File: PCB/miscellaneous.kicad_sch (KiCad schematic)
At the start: 34 parts

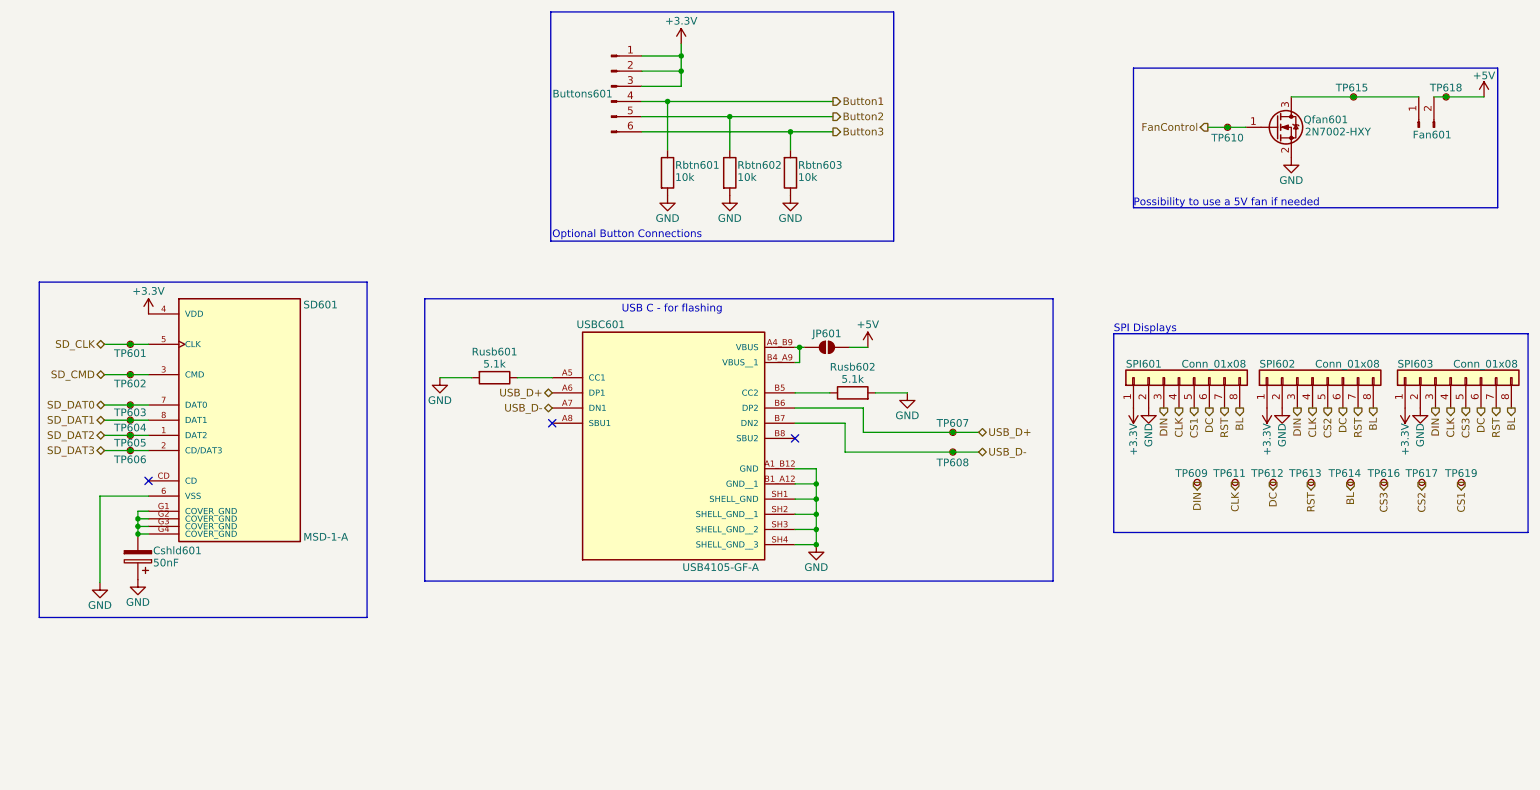
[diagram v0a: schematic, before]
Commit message: Applied recommendations from my coworker; Fixed badly placed filter caps; Added flyback diode to fan circuit; Applied larger grid and some spacing to the schematics; And some other small adjustments
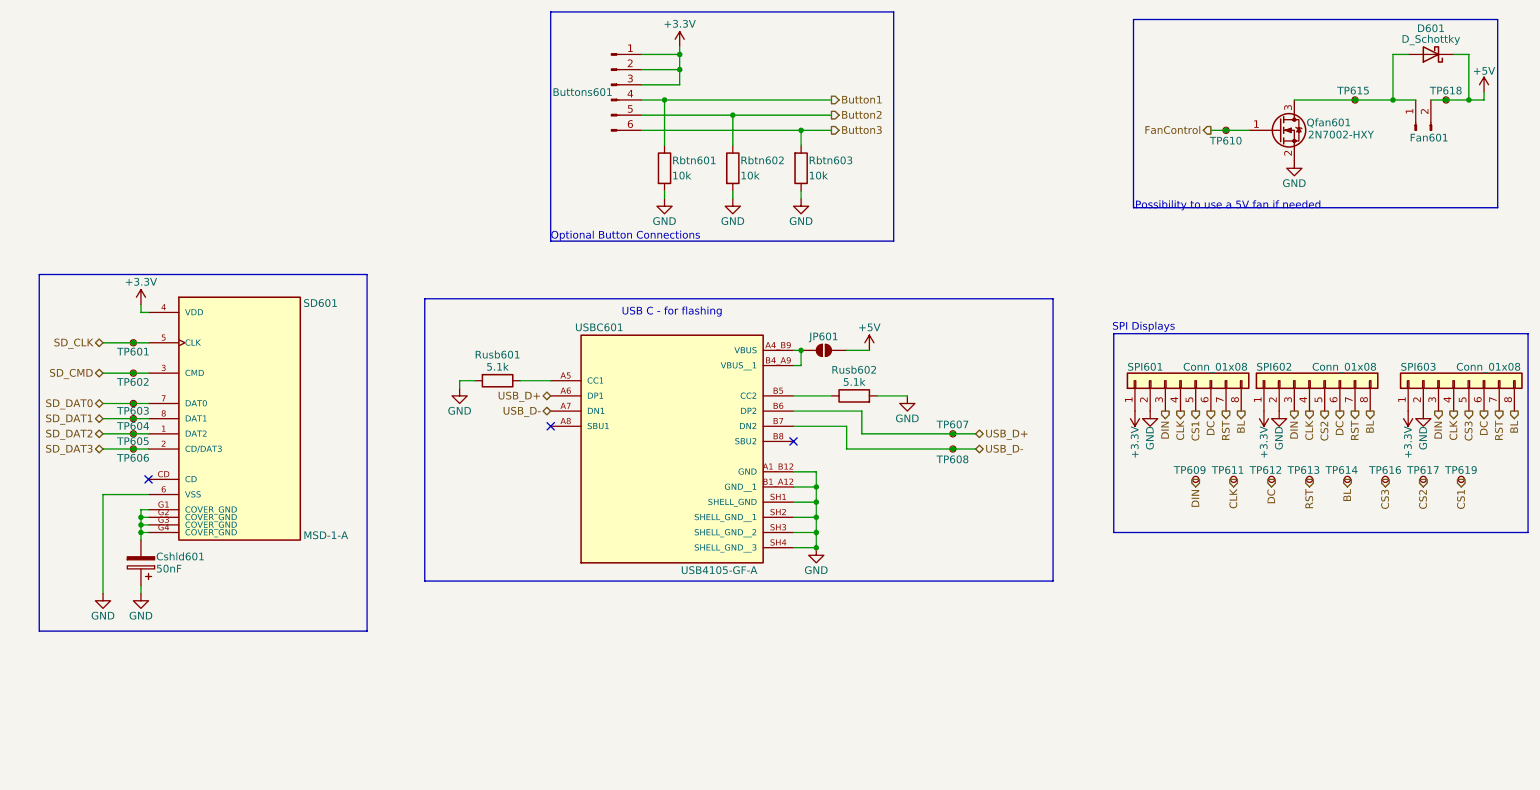
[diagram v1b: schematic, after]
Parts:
- added D601: D_Schottky, Diode_SMD:D_0805_2012Metric, symbol Device:D_Schottky
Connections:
- net +5V: now also D601.1 (K)
- net at Fan601.1 (Pin_1), Qfan601.3 (D), TP615.1: now also D601.2 (A)
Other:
- title: (none) -> Miscellaneous
- moved on the sheet: Cshld601, Fan601, JP601, Qfan601, Rbtn601, Rbtn602, Rbtn603, Rusb601, Rusb602, SPI601, SPI602, SPI603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

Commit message: Changed some resistor and capacitor values;Added additional input electrolytic cap;Selected LCSC parts;Added diode footprint;Removed 3.3V power supply and decreased the output of the 5V supply to 3.3V;Added flyback diode on the fan circuit;Added LDO between the USB-C VBUS and the 5V rail
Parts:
- removed TP618: TestPoint_Small, TestPoint:TestPoint_Pad_D1.0mm, symbol Connector:TestPoint_Small
- added C601: 10uF, Capacitor_SMD:C_0805_2012Metric, symbol Device:C
- added C602: 22uF, Capacitor_SMD:C_0805_2012Metric, symbol Device:C
- added U601: AMS1117-3.3, Package_TO_SOT_SMD:SOT-223-3_TabPin2, symbol Regulator_Linear:AMS1117-3.3
- D601: footprint Diode_SMD:D_0805_2012Metric -> customFootprints:SOD-323HE
- renumbered TP609 to TP601, TP611 to TP602, TP601 to TP603, TP602 to TP604, TP603 to TP605, TP604 to TP606, TP605 to TP607, TP606 to TP608, TP612 to TP609, TP613 to TP610, TP614 to TP611, TP616 to TP612, TP617 to TP613, TP619 to TP614, TP607 to TP615, TP608 to TP616, TP610 to TP617, TP615 to TP618
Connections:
- net +3.3V: now also D601.1 (K), Fan601.2 (Pin_2), C602.1, U601.2 (VO)
- net GND: now also C601.2, C602.2, U601.1 (GND)
- removed net +5V: D601.1 (K), Fan601.2 (Pin_2), JP601.2 (B)
- new net: C601.1, JP601.2 (B), U601.3 (VI)
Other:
- moved on the sheet: JP601, Rusb601, Rusb602, SPI601, SPI602, SPI603, TP601, TP602, TP609, TP610, TP611, TP612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
